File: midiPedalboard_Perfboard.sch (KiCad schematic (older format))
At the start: 47 parts, among them J1 wire, J10 wire, J11 wire, J12 wire, J13 wire, J14 wire, J15 MIDI_4, J16 MIDI_5, J17 MIDI_4, J18 MIDI_2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

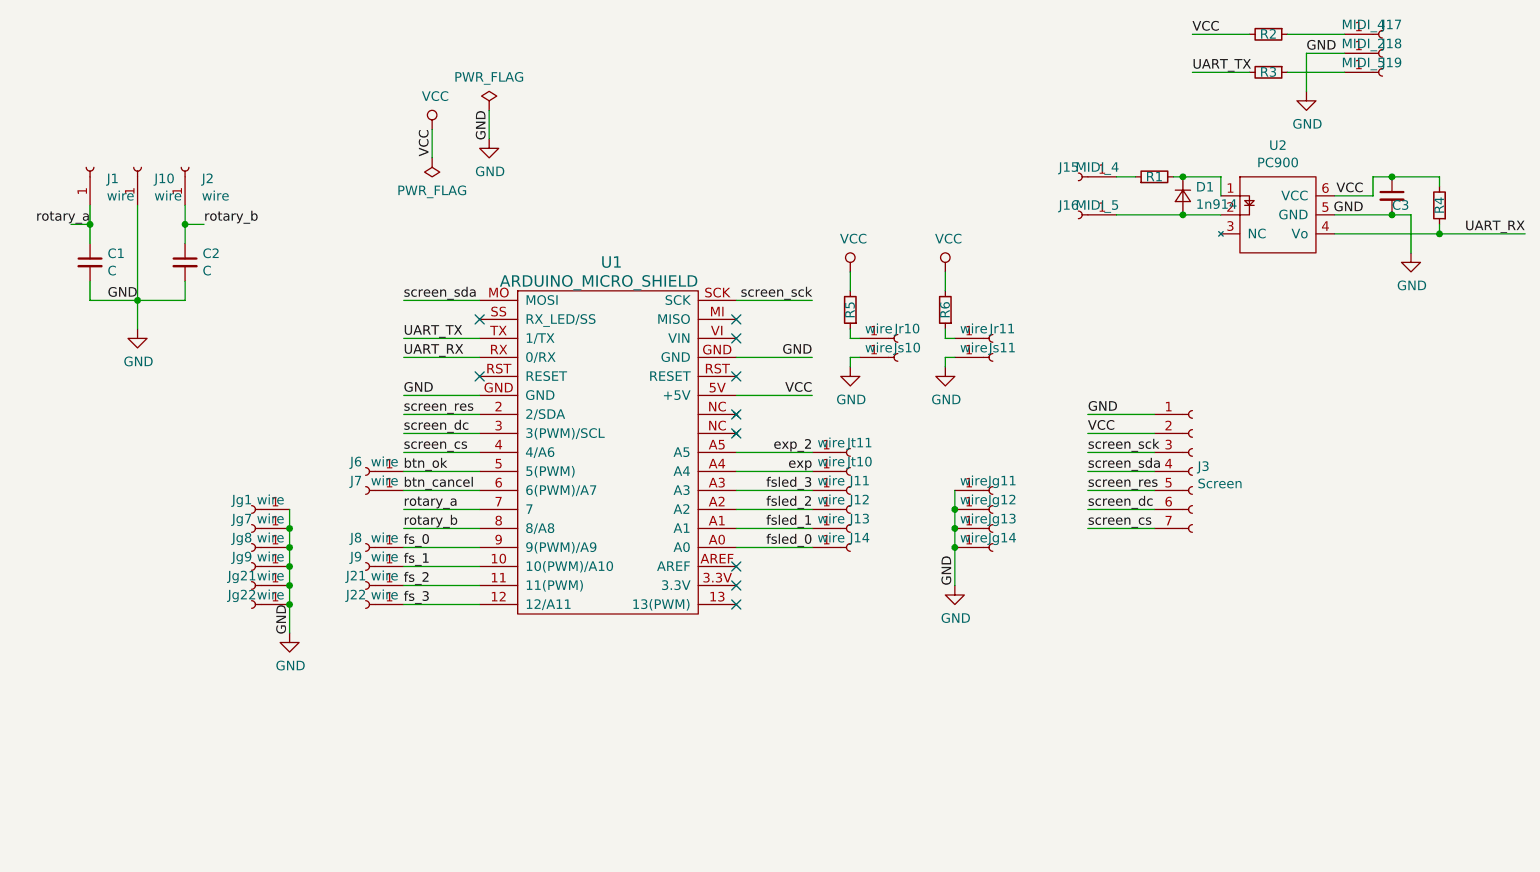
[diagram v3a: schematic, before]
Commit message: condensator for adc filtering
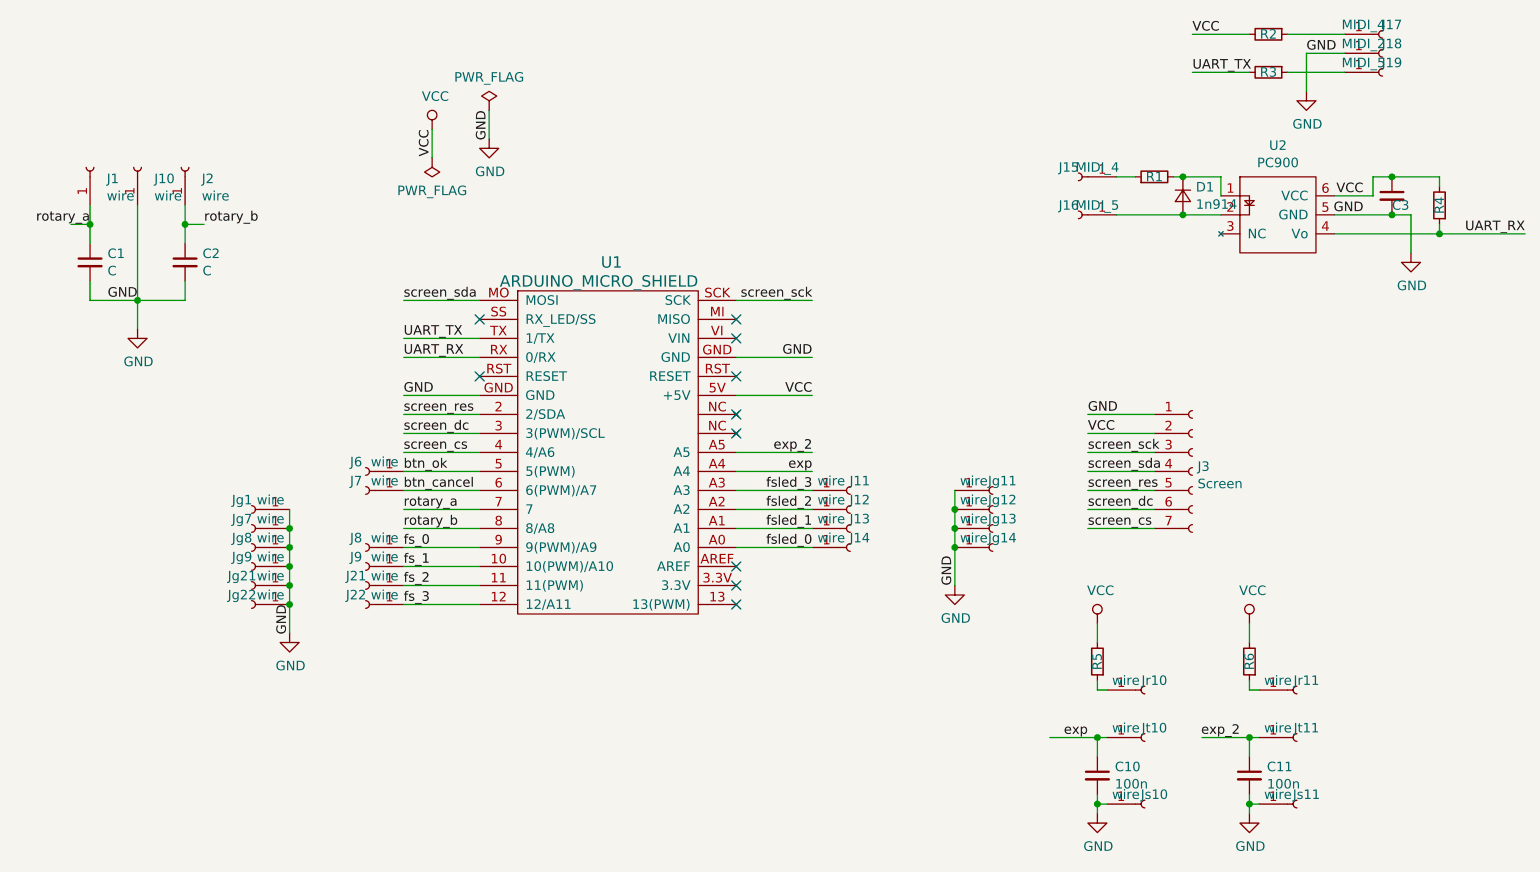
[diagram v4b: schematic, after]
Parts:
- added C10, C11: 100n, Capacitor_THT:C_Rect_L7.0mm_W2.0mm_P5.00mm, symbol Device:C_Small
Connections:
- net GND: now also C10.2, C11.2
- net exp: now also C10.1
- net exp_2: now also C11.1
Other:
- moved on the sheet: Jr10, Jr11, Js10, Js11, Jt10, Jt11, R5, R6
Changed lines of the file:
@@
 Wire Wire Line
 	5900 4000 6300 4000
-Wire Wire Line
-	5900 3600 6300 3600
-Text Label 6300 3600 2    50   ~ 0
+Text Label 7750 5000 2    50   ~ 0
 exp
 Wire Wire Line
@@
 L Connector:Conn_01x01_Female Jt10
 U 1 1 5CAC0FB0
-P 6500 3600
-F 0 "Jt10" H 6550 3650 50  0000 C CNN
-F 1 "wire" H 6400 3650 50  0000 C CNN
-F 2 "Connector_Wire:SolderWirePad_1x01_Drill0.8mm" H 6500 3600 50  0001 C CNN
-F 3 "~" H 6500 3600 50  0001 C CNN
-	1    6500 3600
+P 8050 5000
+F 0 "Jt10" H 8100 5050 50  0000 C CNN
+F 1 "wire" H 7950 5050 50  0000 C CNN
+F 2 "Connector_Wire:SolderWirePad_1x01_Drill0.8mm" H 8050 5000 50  0001 C CNN
+F 3 "~" H 8050 5000 50  0001 C CNN
+	1    8050 5000
 	1    0    0    -1
 $EndComp
@@
 L Connector:Conn_01x01_Female Jr10
 U 1 1 5CAF6041
-P 6750 2900
-F 0 "Jr10" H 6800 2950 50  0000 C CNN
-F 1 "wire" H 6650 2950 50  0000 C CNN
-F 2 "Connector_Wire:SolderWirePad_1x01_Drill0.8mm" H 6750 2900 50  0001 C CNN
-F 3 "~" H 6750 2900 50  0001 C CNN
-	1    6750 2900
+P 8050 4750
+F 0 "Jr10" H 8100 4800 50  0000 C CNN
+F 1 "wire" H 7950 4800 50  0000 C CNN
+F 2 "Connector_Wire:SolderWirePad_1x01_Drill0.8mm" H 8050 4750 50  0001 C CNN
+F 3 "~" H 8050 4750 50  0001 C CNN
+	1    8050 4750
 	1    0    0    -1
 $EndComp
@@
 L Connector:Conn_01x01_Female Js10
 U 1 1 5CAF60E1
-P 6750 3000
-F 0 "Js10" H 6800 3050 50  0000 C CNN
-F 1 "wire" H 6650 3050 50  0000 C CNN
-F 2 "Connector_Wire:SolderWirePad_1x01_Drill0.8mm" H 6750 3000 50  0001 C CNN
-F 3 "~" H 6750 3000 50  0001 C CNN
-	1    6750 3000
+P 8050 5350
+F 0 "Js10" H 8100 5400 50  0000 C CNN
+F 1 "wire" H 7950 5400 50  0000 C CNN
+F 2 "Connector_Wire:SolderWirePad_1x01_Drill0.8mm" H 8050 5350 50  0001 C CNN
+F 3 "~" H 8050 5350 50  0001 C CNN
+	1    8050 5350
 	1    0    0    -1
 $EndComp
@@
 L Device:R_Small R5
 U 1 1 5CAF65EA
-P 6500 2750
-F 0 "R5" V 6500 2750 50  0000 C CNN
-F 1 "100" V 6395 2750 50  0001 C CNN
-F 2 "Resistor_THT:R_Axial_DIN0207_L6.3mm_D2.5mm_P2.54mm_Vertical" H 6500 2750 50  0001 C CNN
-F 3 "~" H 6500 2750 50  0001 C CNN
-	1    6500 2750
+P 7800 4600
+F 0 "R5" V 7800 4600 50  0000 C CNN
+F 1 "100" V 7695 4600 50  0001 C CNN
+F 2 "Resistor_THT:R_Axial_DIN0207_L6.3mm_D2.5mm_P2.54mm_Vertical" H 7800 4600 50  0001 C CNN
+F 3 "~" H 7800 4600 50  0001 C CNN
+	1    7800 4600
 	-1   0    0    1
 $EndComp
@@
 L power:VCC #PWR0109
 U 1 1 5CAF680A
-P 6500 2550
-F 0 "#PWR0109" H 6500 2400 50  0001 C CNN
-F 1 "VCC" H 6517 2723 50  0000 C CNN
-F 2 "" H 6500 2550 50  0001 C CNN
-F 3 "" H 6500 2550 50  0001 C CNN
-	1    6500 2550
-	1    0    0    -1
-$EndComp
-Wire Wire Line
-	6500 2550 6500 2650
-Wire Wire Line
-	6500 2850 6500 2900
-Wire Wire Line
-	6500 2900 6550 2900
-Wire Wire Line
-	6550 3000 6500 3000
-Wire Wire Line
-	6500 3000 6500 3050
+P 7800 4400
+F 0 "#PWR0109" H 7800 4250 50  0001 C CNN
+F 1 "VCC" H 7817 4573 50  0000 C CNN
+F 2 "" H 7800 4400 50  0001 C CNN
+F 3 "" H 7800 4400 50  0001 C CNN
+	1    7800 4400
+	1    0    0    -1
+$EndComp
+Wire Wire Line
+	7800 4400 7800 4500
+Wire Wire Line
+	7800 4700 7800 4750
+Wire Wire Line
+	7800 4750 7850 4750
+Wire Wire Line
+	7850 5350 7800 5350
+Wire Wire Line
+	7800 5350 7800 5400
 $Comp
 L power:GND #PWR0110
 U 1 1 5CAFA231
-P 6500 3050
-F 0 "#PWR0110" H 6500 2800 50  0001 C CNN
-F 1 "GND" H 6505 2877 50  0000 C CNN
-F 2 "" H 6500 3050 50  0001 C CNN
-F 3 "" H 6500 3050 50  0001 C CNN
-	1    6500 3050
+P 7800 5400
+F 0 "#PWR0110" H 7800 5150 50  0001 C CNN
+F 1 "GND" H 7805 5227 50  0000 C CNN
+F 2 "" H 7800 5400 50  0001 C CNN
+F 3 "" H 7800 5400 50  0001 C CNN
+	1    7800 5400
 	1    0    0    -1
 $EndComp
@@
 	1    0    0    -1
 $EndComp
+Text Label 8550 5000 2    50   ~ 0
+exp_2
+$Comp
+L Connector:Conn_01x01_Female Jt11
+U 1 1 5CCAFC10
+P 8850 5000
+F 0 "Jt11" H 8900 5050 50  0000 C CNN
+F 1 "wire" H 8750 5050 50  0000 C CNN
+F 2 "Connector_Wire:SolderWirePad_1x01_Drill0.8mm" H 8850 5000 50  0001 C CNN
+F 3 "~" H 8850 5000 50  0001 C CNN
+	1    8850 5000
+	1    0    0    -1
+$EndComp
+$Comp
+L Connector:Conn_01x01_Female Jr11
+U 1 1 5CCBBBC1
+P 8850 4750
+F 0 "Jr11" H 8900 4800 50  0000 C CNN
+F 1 "wire" H 8750 4800 50  0000 C CNN
+F 2 "Connector_Wire:SolderWirePad_1x01_Drill0.8mm" H 8850 4750 50  0001 C CNN
+F 3 "~" H 8850 4750 50  0001 C CNN
+	1    8850 4750
+	1    0    0    -1
+$EndComp
+$Comp
+L Connector:Conn_01x01_Female Js11
+U 1 1 5CCBBBC8
+P 8850 5350
+F 0 "Js11" H 8900 5400 50  0000 C CNN
+F 1 "wire" H 8750 5400 50  0000 C CNN
+F 2 "Connector_Wire:SolderWirePad_1x01_Drill0.8mm" H 8850 5350 50  0001 C CNN
+F 3 "~" H 8850 5350 50  0001 C CNN
+	1    8850 5350
+	1    0    0    -1
+$EndComp
+$Comp
+L Device:R_Small R6
+U 1 1 5CCBBBCF
+P 8600 4600
+F 0 "R6" V 8600 4600 50  0000 C CNN
+F 1 "100" V 8495 4600 50  0001 C CNN
+F 2 "Resistor_THT:R_Axial_DIN0207_L6.3mm_D2.5mm_P2.54mm_Vertical" H 8600 4600 50  0001 C CNN
+F 3 "~" H 8600 4600 50  0001 C CNN
+	1    8600 4600
+	-1   0    0    1
+$EndComp
+$Comp
+L power:VCC #PWR0101
+U 1 1 5CCBBBD6
+P 8600 4400
+F 0 "#PWR0101" H 8600 4250 50  0001 C CNN
+F 1 "VCC" H 8617 4573 50  0000 C CNN
+F 2 "" H 8600 4400 50  0001 C CNN
+F 3 "" H 8600 4400 50  0001 C CNN
+	1    8600 4400
+	1    0    0    -1
+$EndComp
+Wire Wire Line
+	8600 4400 8600 4500
+Wire Wire Line
+	8600 4700 8600 4750
+Wire Wire Line
+	8600 4750 8650 4750
+Wire Wire Line
+	8650 5350 8600 5350
+Wire Wire Line
+	8600 5350 8600 5400
+$Comp
+L power:GND #PWR0111
+U 1 1 5CCBBBE1
+P 8600 5400
+F 0 "#PWR0111" H 8600 5150 50  0001 C CNN
+F 1 "GND" H 8605 5227 50  0000 C CNN
+F 2 "" H 8600 5400 50  0001 C CNN
+F 3 "" H 8600 5400 50  0001 C CNN
+	1    8600 5400
+	1    0    0    -1
+$EndComp
 Wire Wire Line
 	5900 3500 6300 3500
+Wire Wire Line
+	5900 3600 6300 3600
+$Comp
+L Device:C_Small C11
+U 1 1 5D1F9307
+P 8600 5200
+F 0 "C11" H 8692 5246 50  0000 L CNN
+F 1 "100n" H 8692 5155 50  0000 L CNN
+F 2 "Capacitor_THT:C_Rect_L7.0mm_W2.0mm_P5.00mm" H 8600 5200 50  0001 C CNN
+F 3 "~" H 8600 5200 50  0001 C CNN
+	1    8600 5200
+	1    0    0    -1
+$EndComp
+$Comp
+L Device:C_Small C10
+U 1 1 5D1F949D
+P 7800 5200
+F 0 "C10" H 7892 5246 50  0000 L CNN
+F 1 "100n" H 7892 5155 50  0000 L CNN
+F 2 "Capacitor_THT:C_Rect_L7.0mm_W2.0mm_P5.00mm" H 7800 5200 50  0001 C CNN
+F 3 "~" H 7800 5200 50  0001 C CNN
+	1    7800 5200
+	1    0    0    -1
+$EndComp
+Wire Wire Line
+	7800 5300 7800 5350
+Connection ~ 7800 5350
+Wire Wire Line
+	8600 5300 8600 5350
+Connection ~ 8600 5350
+Wire Wire Line
+	8600 5000 8600 5100
+Connection ~ 8600 5000
+Wire Wire Line
+	8600 5000 8650 5000
+Wire Wire Line
+	8350 5000 8600 5000
+Wire Wire Line
+	7800 5100 7800 5000
+Connection ~ 7800 5000
+Wire Wire Line
+	7800 5000 7850 5000
+Wire Wire Line
+	7550 5000 7800 5000
+Text Label 6300 3600 2    50   ~ 0
+exp
 Text Label 6300 3500 2    50   ~ 0
 exp_2
-$Comp
-L Connector:Conn_01x01_Female Jt11
-U 1 1 5CCAFC10
-P 6500 3500
-F 0 "Jt11" H 6550 3550 50  0000 C CNN
-F 1 "wire" H 6400 3550 50  0000 C CNN
-F 2 "Connector_Wire:SolderWirePad_1x01_Drill0.8mm" H 6500 3500 50  0001 C CNN
-F 3 "~" H 6500 3500 50  0001 C CNN
-	1    6500 3500
-	1    0    0    -1
-$EndComp
-$Comp
-L Connector:Conn_01x01_Female Jr11
-U 1 1 5CCBBBC1
-P 7250 2900
-F 0 "Jr11" H 7300 2950 50  0000 C CNN
-F 1 "wire" H 7150 2950 50  0000 C CNN
-F 2 "Connector_Wire:SolderWirePad_1x01_Drill0.8mm" H 7250 2900 50  0001 C CNN
-F 3 "~" H 7250 2900 50  0001 C CNN
-	1    7250 2900
-	1    0    0    -1
-$EndComp
-$Comp
-L Connector:Conn_01x01_Female Js11
-U 1 1 5CCBBBC8
-P 7250 3000
-F 0 "Js11" H 7300 3050 50  0000 C CNN
-F 1 "wire" H 7150 3050 50  0000 C CNN
-F 2 "Connector_Wire:SolderWirePad_1x01_Drill0.8mm" H 7250 3000 50  0001 C CNN
-F 3 "~" H 7250 3000 50  0001 C CNN
-	1    7250 3000
-	1    0    0    -1
-$EndComp
-$Comp
-L Device:R_Small R6
-U 1 1 5CCBBBCF
-P 7000 2750
-F 0 "R6" V 7000 2750 50  0000 C CNN
-F 1 "100" V 6895 2750 50  0001 C CNN
-F 2 "Resistor_THT:R_Axial_DIN0207_L6.3mm_D2.5mm_P2.54mm_Vertical" H 7000 2750 50  0001 C CNN
-F 3 "~" H 7000 2750 50  0001 C CNN
-	1    7000 2750
-	-1   0    0    1
-$EndComp
-$Comp
-L power:VCC #PWR0101
-U 1 1 5CCBBBD6
-P 7000 2550
-F 0 "#PWR0101" H 7000 2400 50  0001 C CNN
-F 1 "VCC" H 7017 2723 50  0000 C CNN
-F 2 "" H 7000 2550 50  0001 C CNN
-F 3 "" H 7000 2550 50  0001 C CNN
-	1    7000 2550
-	1    0    0    -1
-$EndComp
-Wire Wire Line
-	7000 2550 7000 2650
-Wire Wire Line
-	7000 2850 7000 2900
-Wire Wire Line
-	7000 2900 7050 2900
-Wire Wire Line
-	7050 3000 7000 3000
-Wire Wire Line
-	7000 3000 7000 3050
-$Comp
-L power:GND #PWR0111
-U 1 1 5CCBBBE1
-P 7000 3050
-F 0 "#PWR0111" H 7000 2800 50  0001 C CNN
-F 1 "GND" H 7005 2877 50  0000 C CNN
-F 2 "" H 7000 3050 50  0001 C CNN
-F 3 "" H 7000 3050 50  0001 C CNN
-	1    7000 3050
-	1    0    0    -1
-$EndComp
 $EndSCHEMATC

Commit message: revert order of fs pin to reflect what i really did
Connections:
- net fs_0: now also J22.1 (Pin_1), U1.12 (12/A11); no longer J8.1 (Pin_1), U1.9 (9(PWM)/A9)
- net fs_1: now also J21.1 (Pin_1), U1.11 (11(PWM)); no longer J9.1 (Pin_1), U1.10 (10(PWM)/A10)
- net fs_2: now also J9.1 (Pin_1), U1.10 (10(PWM)/A10); no longer J21.1 (Pin_1), U1.11 (11(PWM))
- net fs_3: now also J8.1 (Pin_1), U1.9 (9(PWM)/A9); no longer J22.1 (Pin_1), U1.12 (12/A11)
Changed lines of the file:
@@
 Text Label 4150 3700 0    50   ~ 0
 btn_cancel
+Text Label 4150 4300 0    50   ~ 0
+fs_0
+Text Label 4150 4200 0    50   ~ 0
+fs_1
+Text Label 4150 4100 0    50   ~ 0
+fs_2
 Text Label 4150 4000 0    50   ~ 0
-fs_0
-Text Label 4150 4100 0    50   ~ 0
-fs_1
-Text Label 4150 4200 0    50   ~ 0
-fs_2
-Text Label 4150 4300 0    50   ~ 0
 fs_3
 NoConn ~ 5900 3300
